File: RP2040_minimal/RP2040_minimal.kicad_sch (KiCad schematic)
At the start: 30 parts, among them J1 USB_C_Receptacle_USB2.0, J2 Conn_01x02, J3 Conn_01x16, J4 Conn_01x16, U1 AP2112K-3.3, U2 W25Q128JVS, U3 RP2040, Y1 445C25D12M00000

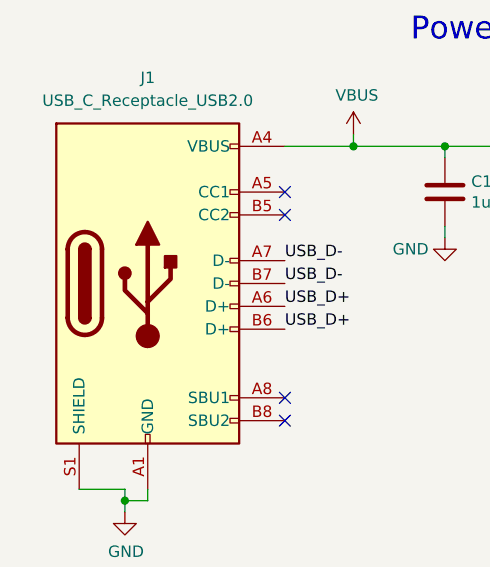
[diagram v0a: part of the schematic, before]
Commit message: Completed routing
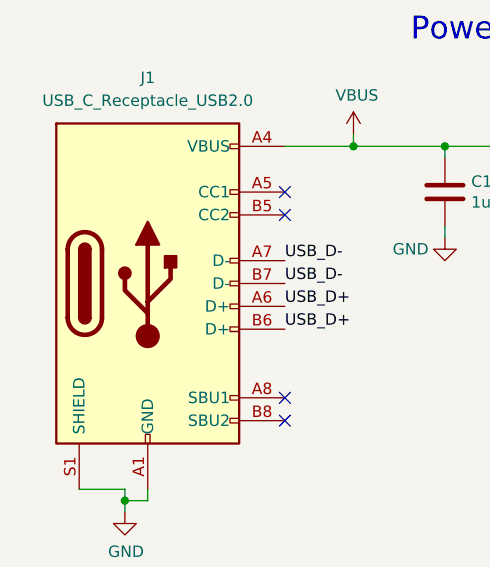
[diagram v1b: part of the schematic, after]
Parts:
- J2: footprint Connector_PinHeader_2.54mm:PinHeader_1x02_P2.54mm_Vertical -> Connector_PinHeader_1.27mm:PinHeader_1x02_P1.27mm_Vertical

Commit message: Switch to 3/5mm vias
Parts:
- removed R2: DNF, Capacitor_SMD:C_0402_1005Metric, symbol Device:R
- added R6, R7: 5.1k, Capacitor_SMD:C_0402_1005Metric, symbol Device:R
- J1: footprint Connector_USB:USB_C_Receptacle_GCT_USB4115-03-C -> Connector_USB:USB_C_Receptacle_G-Switch_GT-USB-7051x
- U2: value W25Q128JVS -> W25Q16JVSNIQ
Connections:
- net GND: now also R6.1, R7.1
- net at J1.A5 (CC1): now also R6.2
- net at J1.B5 (CC2): now also R7.2
- no-connect marks 5 -> 3
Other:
- moved on the sheet: C1, C4, U1

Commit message: v1.0 submitted for manufacture
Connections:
- net A0: now also U3.2 (GPIO0); no longer U3.13 (GPIO10)
- net A1: now also U3.3 (GPIO1); no longer U3.12 (GPIO9)
- net A10: now also U3.13 (GPIO10); no longer U3.14 (GPIO11)
- net A11: now also U3.14 (GPIO11); no longer U3.15 (GPIO12)
- net A12: now also U3.15 (GPIO12); no longer U3.4 (GPIO2)
- net A13: now also U3.16 (GPIO13); no longer U3.18 (GPIO15)
- net A14: now also U3.17 (GPIO14); no longer U3.27 (GPIO16)
- net A15: now also U3.18 (GPIO15); no longer U3.3 (GPIO1)
- net A16: now also U3.27 (GPIO16); no longer U3.2 (GPIO0)
- net A2: now also U3.4 (GPIO2); no longer U3.11 (GPIO8)
- net A3: now also U3.5 (GPIO3); no longer U3.9 (GPIO7)
- net A4: now also U3.6 (GPIO4); no longer U3.8 (GPIO6)
- net A6: now also U3.8 (GPIO6); no longer U3.6 (GPIO4)
- net A7: now also U3.9 (GPIO7); no longer U3.5 (GPIO3)
- net A8: now also U3.11 (GPIO8); no longer U3.17 (GPIO14)
- net A9: now also U3.12 (GPIO9); no longer U3.16 (GPIO13)
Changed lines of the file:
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@@
     (effects (font (size 1.27 1.27)) (justify right bottom))
   )
-  (label "A2" (at 245.11 132.08 180) (fields_autoplaced)
+  (label "A8" (at 245.11 132.08 180) (fields_autoplaced)
     (effects (font (size 1.27 1.27)) (justify right bottom))
   )
@@
     (effects (font (size 1.27 1.27)) (justify left bottom))
   )
-  (label "A15" (at 245.11 114.3 180) (fields_autoplaced)
+  (label "A1" (at 245.11 114.3 180) (fields_autoplaced)
     (effects (font (size 1.27 1.27)) (justify right bottom))
   )
@@
     (effects (font (size 1.27 1.27)) (justify right bottom))
   )
-  (label "A16" (at 245.11 111.76 180) (fields_autoplaced)
+  (label "A0" (at 245.11 111.76 180) (fields_autoplaced)
     (effects (font (size 1.27 1.27)) (justify right bottom))
   )
@@
     (effects (font (size 1.27 1.27)) (justify right bottom))
   )
-  (label "A12" (at 245.11 116.84 180) (fields_autoplaced)
+  (label "A2" (at 245.11 116.84 180) (fields_autoplaced)
     (effects (font (size 1.27 1.27)) (justify right bottom))
   )
@@
     (effects (font (size 1.27 1.27)) (justify right bottom))
   )
-  (label "A10" (at 245.11 139.7 180) (fields_autoplaced)
+  (label "A11" (at 245.11 139.7 180) (fields_autoplaced)
     (effects (font (size 1.27 1.27)) (justify right bottom))
   )
@@
     (effects (font (size 1.27 1.27)) (justify right bottom))
   )
-  (label "A0" (at 245.11 137.16 180) (fields_autoplaced)
+  (label "A10" (at 245.11 137.16 180) (fields_autoplaced)
     (effects (font (size 1.27 1.27)) (justify right bottom))
   )
@@
     (effects (font (size 1.27 1.27)) (justify right bottom))
   )
-  (label "A11" (at 245.11 142.24 180) (fields_autoplaced)
+  (label "A12" (at 245.11 142.24 180) (fields_autoplaced)
     (effects (font (size 1.27 1.27)) (justify right bottom))
   )
@@
     (effects (font (size 1.27 1.27)) (justify right bottom))
   )
-  (label "A6" (at 245.11 121.92 180) (fields_autoplaced)
-    (effects (font (size 1.27 1.27)) (justify right bottom))
-  )
-  (label "A9" (at 245.11 144.78 180) (fields_autoplaced)
+  (label "A4" (at 245.11 121.92 180) (fields_autoplaced)
+    (effects (font (size 1.27 1.27)) (justify right bottom))
+  )
+  (label "A13" (at 245.11 144.78 180) (fields_autoplaced)
     (effects (font (size 1.27 1.27)) (justify right bottom))
   )
@@
     (effects (font (size 1.27 1.27)) (justify right bottom))
   )
-  (label "A13" (at 245.11 149.86 180) (fields_autoplaced)
+  (label "A15" (at 245.11 149.86 180) (fields_autoplaced)
     (effects (font (size 1.27 1.27)) (justify right bottom))
   )
@@
     (effects (font (size 1.27 1.27)) (justify left bottom))
   )
-  (label "A14" (at 245.11 152.4 180) (fields_autoplaced)
-    (effects (font (size 1.27 1.27)) (justify right bottom))
-  )
-  (label "A8" (at 245.11 147.32 180) (fields_autoplaced)
+  (label "A16" (at 245.11 152.4 180) (fields_autoplaced)
+    (effects (font (size 1.27 1.27)) (justify right bottom))
+  )
+  (label "A14" (at 245.11 147.32 180) (fields_autoplaced)
     (effects (font (size 1.27 1.27)) (justify right bottom))
   )
@@
     (effects (font (size 1.27 1.27)) (justify left bottom))
   )
-  (label "A4" (at 245.11 127 180) (fields_autoplaced)
-    (effects (font (size 1.27 1.27)) (justify right bottom))
-  )
-  (label "A3" (at 245.11 129.54 180) (fields_autoplaced)
+  (label "A6" (at 245.11 127 180) (fields_autoplaced)
+    (effects (font (size 1.27 1.27)) (justify right bottom))
+  )
+  (label "A7" (at 245.11 129.54 180) (fields_autoplaced)
     (effects (font (size 1.27 1.27)) (justify right bottom))
   )
@@
     (effects (font (size 1.27 1.27)) (justify right bottom))
   )
-  (label "A7" (at 245.11 119.38 180) (fields_autoplaced)
+  (label "A3" (at 245.11 119.38 180) (fields_autoplaced)
     (effects (font (size 1.27 1.27)) (justify right bottom))
   )
@@
     (effects (font (size 1.27 1.27)) (justify right bottom))
   )
-  (label "A1" (at 245.11 134.62 180) (fields_autoplaced)
-    (effects (font (size 1.27 1.27)) (justify right bottom))
-  )
+  (label "A9" (at 245.11 134.62 180) (fields_autoplaced)
+    (effects (font (size 1.27 1.27)) (justify right bottom))
+  )
